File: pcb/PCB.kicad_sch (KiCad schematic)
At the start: 35 parts, among them J1 Conn_01x15, J2 USB_C_Receptacle_USB2.0, J3 Conn_01x15, J4 TC2030, J5 Conn_01x04, SW1 SW_Push, SW2 SW_Push, U1 SN65HVD230, U2 AMS1117-3.3, U3 STM32F103C8T6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

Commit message: Finished schematic
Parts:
- removed C10, C12, C8, C9: 100n, Capacitor_SMD:C_0402_1005Metric, symbol Device:C_Small
- removed C11, C2: 1u, Capacitor_SMD:C_0603_1608Metric, symbol Device:C_Small
- removed C5: 30p, Capacitor_SMD:C_0402_1005Metric, symbol Device:C_Small
- removed D1: YELLOW, LED_SMD:LED_0603_1608Metric, symbol Device:LED_Small
- removed D2: BLUE, LED_SMD:LED_0603_1608Metric, symbol Device:LED_Small
- removed FB1, FB2: 100R@100MHz, Resistor_SMD:R_0805_2012Metric, symbol Device:FerriteBead_Small
- removed J1, J3: Conn_01x15, Connector_PinHeader_2.54mm:PinHeader_1x15_P2.54mm_Vertical, symbol Connector_Generic:Conn_01x15
- removed J2: USB_C_Receptacle_USB2.0, Connector_USB:USB_C_Receptacle_HRO_TYPE-C-31-M-12, symbol Connector:USB_C_Receptacle_USB2.0
- removed J4: TC2030, Connector:Tag-Connect_TC2030-IDC-NL_2x03_P1.27mm_Vertical, symbol TC2030:TC2030
- removed J5: Conn_01x04, Connector_PinHeader_2.54mm:PinHeader_1x04_P2.54mm_Vertical, symbol Connector_Generic:Conn_01x04
- removed JP1: SolderJumper_Bridged, Jumper:SolderJumper-2_P1.3mm_Bridged_RoundedPad1.0x1.5mm, symbol Jumper:SolderJumper_2_Bridged
- removed R3: 120R, Resistor_SMD:R_0402_1005Metric, symbol Device:R_Small
- removed R4, R6, R7: 1k5, Resistor_SMD:R_0402_1005Metric, symbol Device:R_Small
- removed R5: 5k1, Resistor_SMD:R_0402_1005Metric, symbol Device:R_Small
- removed SW1, SW2: SW_Push, Button_Switch_SMD:SW_Push_1P1T_NO_CK_KSC7xxJ, symbol Switch:SW_Push
- removed U3: STM32F103C8T6, Package_QFP:LQFP-48_7x7mm_P0.5mm, symbol MCU_ST_STM32F1:STM32F103C8Tx
- removed Y1: 8MHz, Crystal:Crystal_SMD_5032-2Pin_5.0x3.2mm, symbol Device:Crystal_Small
- added C2, C5: 100uF, Capacitor_SMD:CP_Elec_6.3x7.7, symbol Device:C_Polarized_Small_US
- added D1: 15-25V, Diode_SMD:D_SMA, symbol Device:D_TVS
- added D16, D2: SP0502BAHT, Package_TO_SOT_SMD:SOT-23, symbol Power_Protection:SP0502BAHT
- added D3: ESDCAN02-2BWY, Package_TO_SOT_SMD:SOT-23, symbol Power_Protection:NUP2105L
- added J1: DTM1312PA12PBR008, DTM13-12PA-12PB:TE_DTM1312PA12PBR008, symbol DTM1312PA12PBR008:DTM1312PA12PBR008
- added R46: 470, Resistor_SMD:R_0603_1608Metric, symbol Device:R_Small
- C3: value 1u -> 2.2uF; footprint Capacitor_SMD:C_0603_1608Metric -> Capacitor_SMD:C_0805_2012Metric; LCSC C15849 -> (none)
- C4: value 4u7 -> 100nF; LCSC C19666 -> (none)
- C7: value 30p -> 100nF; footprint Capacitor_SMD:C_0402_1005Metric -> Capacitor_SMD:C_0603_1608Metric; LCSC C1570 -> (none)
- R1, R2: value 5k1 -> 470; footprint Resistor_SMD:R_0402_1005Metric -> Resistor_SMD:R_0603_1608Metric; LCSC C25905 -> (none)
- U2: LCSC C6186 -> (none)
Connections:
- net HSE_IN is gone; now on net +3V3: C7.1
- net +3V3: now also C5.1; no longer C3.1, C4.1, C6.1
- net CAN+: now also D3.1 (K), J1.B5
- net CAN-: now also D3.2 (K), J1.B6
- net GND: now also C2.2, C5.2, D1.2 (A2), D16.3 (A), D2.3 (A), J1.A11, J1.A2, J1.B10, J1.B3; no longer C6.2, R1.2, R2.1
- net UART_TX: now reaches R1.1
- net UART_TX: now also D2.1 (K), J1.B7
- net UART_RX: now reaches R2.2
- net UART_RX: now also D2.2 (K), J1.B8
- net at U1.5 (Vref): now also C6.1
- net VCC renamed +12V
- net +12V: now also C3.1, C4.1, C2.1, D1.1 (A1), J1.A10, J1.A3, J1.B4
- new net: C6.2, D3.3 (A)
- new net H0: J1.A12
- new net H1: J1.B1
- new net H2: J1.B2
- new net H3: J1.B11
- new net H4: J1.B12
- new net H5: J1.A1
- new net IO: D16.2 (K), J1.B9, R46.2
- new net L0: J1.A7
- new net L1: J1.A6
- new net L2: J1.A8
- new net L3: J1.A5
- new net L4: J1.A9
- new net L5: J1.A4
- new net STM32/GPIO: R46.1
- new net STM32/UART_RX: R2.1
- new net STM32/UART_TX: R1.2
- no-connect marks 9 -> 1
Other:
- added sheet High-side Channel 0 (highside.kicad_sch)
- added sheet High-side Channel 1 (highside.kicad_sch)
- added sheet High-side Channel 2 (highside.kicad_sch)
- added sheet High-side Channel 3 (highside.kicad_sch)
- added sheet High-side Channel 4 (highside.kicad_sch)
- added sheet High-side Channel 5 (highside.kicad_sch)
- added sheet Low-side channel 0 (lowside.kicad_sch)
- added sheet Low-side channel 1 (lowside.kicad_sch)
- added sheet Low-side channel 2 (lowside.kicad_sch)
- added sheet Low-side channel 3 (lowside.kicad_sch)
- added sheet Low-side channel 4 (lowside.kicad_sch)
- added sheet Low-side channel 5 (lowside.kicad_sch)
- added sheet STM32 (STM32.kicad_sch)
- note added: "3.3V Regulator"
- note removed: "1 = Bootloader, 0 = 'Run'"
- note removed: "1x bulk decoupling + 100nF per VDD pin"
- note removed: "3V3 regulator stable with 1uF output cap."
- note removed: "CL = 2 * (Cload - Cstray)"
- note removed: "GPIO Headers"
- note removed: "Ideally, boards should include GND for each signal pin and decoupling at power output pins (like +3V3)."
- note removed: "Low-pass filter for analog VDD"
- note removed: "Note: Best practice is to include a TVS protection diode near the connector (Refer to BCM design)."
- note removed: "Note: Power flags tell KiCad that a net is a power source. This avoids errors during Electrical Rules Check."
- note removed: "Optional termination resistor. See Brake Light schematic for a reference split-terminated design."
- note removed: "Programming/debug header. Place in an accessible location close to the mcu."
- note removed: "STM32F1 Microcontroller"
- note removed: "STM32F103 Reference Breakout Board"
- note removed: "STM32F103 requires external 1k5 pull-up on USB D+ line."
- note removed: "Tag Connect"
- note removed: "USB and Regulator"
- note removed: "USB device - leave shield floating."
- moved on the sheet: C1, U1

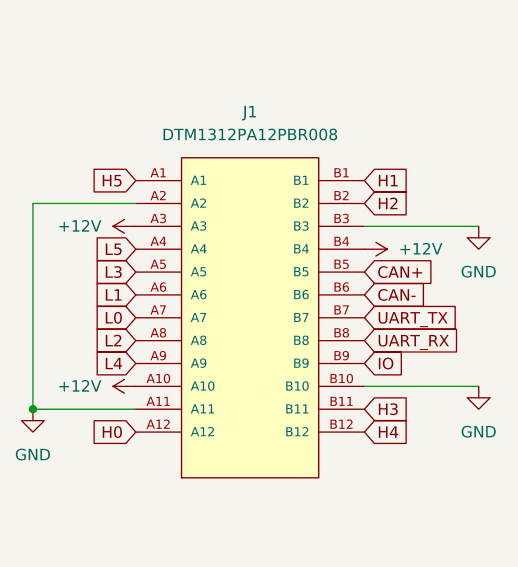
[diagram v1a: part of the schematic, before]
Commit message: Started layout
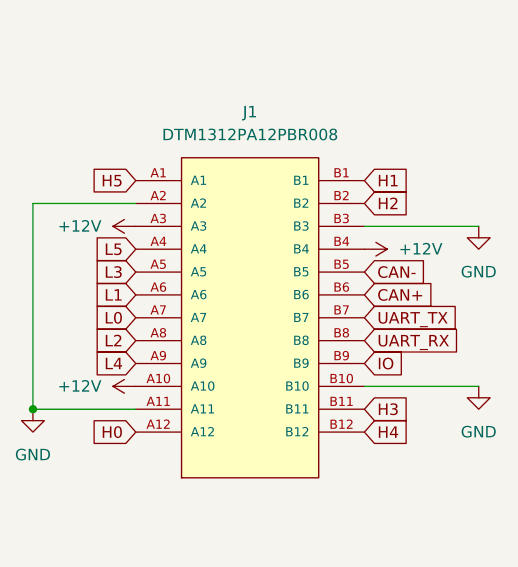
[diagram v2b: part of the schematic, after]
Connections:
- net CAN+: now also J1.B6; no longer J1.B5
- net CAN-: now also J1.B5; no longer J1.B6
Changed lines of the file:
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@@
     )
   )
-  (global_label "CAN-" (shape input) (at 234.95 87.63 0) (fields_autoplaced)
-    (effects (font (size 1.27 1.27)) (justify left))
-    (property "Intersheet References" "${INTERSHEET_REFS}" (id 0) (at 242.6245 87.5506 0)
+  (global_label "CAN-" (shape input) (at 234.95 85.09 0) (fields_autoplaced)
+    (effects (font (size 1.27 1.27)) (justify left))
+    (property "Intersheet References" "${INTERSHEET_REFS}" (id 0) (at 242.6245 85.0106 0)
       (effects (font (size 1.27 1.27)) (justify left) hide)
     )
@@
     )
   )
-  (global_label "CAN+" (shape input) (at 234.95 85.09 0) (fields_autoplaced)
-    (effects (font (size 1.27 1.27)) (justify left))
-    (property "Intersheet References" "${INTERSHEET_REFS}" (id 0) (at 242.6245 85.0106 0)
+  (global_label "CAN+" (shape input) (at 234.95 87.63 0) (fields_autoplaced)
+    (effects (font (size 1.27 1.27)) (justify left))
+    (property "Intersheet References" "${INTERSHEET_REFS}" (id 0) (at 242.6245 87.5506 0)
       (effects (font (size 1.27 1.27)) (justify left) hide)
     )
@@
       (reference "#PWR010") (unit 1) (value "+3V3") (footprint "")
     )
-    (path "/1d08d960-24a6-461a-b4f3-543e0f014558/898ca406-6b9b-4516-8b9f-8dbe52b67a30"
-      (reference "#PWR011") (unit 1) (value "+3V3") (footprint "")
-    )
     (path "/1d08d960-24a6-461a-b4f3-543e0f014558/cdb9daf3-cf5d-4c6d-be96-1ffa36850e9c"
       (reference "#PWR012") (unit 1) (value "GND") (footprint "")
@@
       (reference "#PWR016") (unit 1) (value "GND") (footprint "")
     )
-    (path "/1d08d960-24a6-461a-b4f3-543e0f014558/8d4a818a-3390-4839-a6b7-95b9c5c5c590"
-      (reference "#PWR017") (unit 1) (value "+3V3") (footprint "")
-    )
     (path "/1d08d960-24a6-461a-b4f3-543e0f014558/4f03b956-f8f7-4414-a0fd-bef829742b97"
       (reference "#PWR018") (unit 1) (value "+3V3") (footprint "")
@@
       (reference "#PWR0107") (unit 1) (value "GND") (footprint "")
     )
+    (path "/1d08d960-24a6-461a-b4f3-543e0f014558/06a93daa-b6e2-4fc1-8d56-459e69185f23"
+      (reference "#PWR?") (unit 1) (value "+3V3") (footprint "")
+    )
     (path "/f95b01db-0883-42ec-8156-6165babeddd5"
       (reference "C1") (unit 1) (value "100n") (footprint "Capacitor_SMD:C_0402_1005Metric")
@@
       (reference "R2") (unit 1) (value "470") (footprint "Resistor_SMD:R_0603_1608Metric")
     )
-    (path "/1d08d960-24a6-461a-b4f3-543e0f014558/0131c735-2ce0-4af4-b13f-c6cd7605fdbe"
-      (reference "R3") (unit 1) (value "5k1") (footprint "Resistor_SMD:R_0603_1608Metric")
-    )
     (path "/ae4e646b-9a05-48be-bf6c-68da84d9d52e/8b021fae-fb4b-4f70-a5f9-b9a251a77706"
       (reference "R4") (unit 1) (value "4.7k") (footprint "Resistor_SMD:R_0603_1608Metric")
@@
       (reference "R46") (unit 1) (value "470") (footprint "Resistor_SMD:R_0603_1608Metric")
     )
-    (path "/1d08d960-24a6-461a-b4f3-543e0f014558/05d4e824-5e78-44e6-a3d5-56fd3c2fb254"
-      (reference "SW1") (unit 1) (value "SW_Push") (footprint "Button_Switch_SMD:SW_Push_1P1T_NO_CK_KSC7xxJ")
-    )
-    (path "/1d08d960-24a6-461a-b4f3-543e0f014558/5248a7c9-e2fa-4657-959b-22392763c96f"
-      (reference "SW2") (unit 1) (value "SW_Push") (footprint "Button_Switch_SMD:SW_Push_1P1T_NO_CK_KSC7xxJ")
-    )
     (path "/ae917481-13f0-43e4-9745-414651f8776f"

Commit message: Worked on layout
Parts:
- renumbered C2 to C1, C1 to C2, D16 to D4, R46 to R3

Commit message: Worked on layout some more
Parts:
- added H1: MountingHole, MountingHole:MountingHole_3.2mm_M3, symbol Mechanical:MountingHole
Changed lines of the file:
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@@
     (pin "2")
+  )
+  (symbol (lib_id "Mechanical:MountingHole") (at 213.36 114.3 0) (unit 1)
+    (in_bom yes) (on_board yes) (fields_autoplaced)
+    (property "Reference" "H1" (id 0) (at 215.9 113.0299 0)
+      (effects (font (size 1.27 1.27)) (justify left))
+    )
+    (property "Value" "MountingHole" (id 1) (at 215.9 115.5699 0)
+      (effects (font (size 1.27 1.27)) (justify left))
+    )
+    (property "Footprint" "MountingHole:MountingHole_3.2mm_M3" (id 2) (at 213.36 114.3 0)
+      (effects (font (size 1.27 1.27)) hide)
+    )
+    (property "Datasheet" "~" (id 3) (at 213.36 114.3 0)
+      (effects (font (size 1.27 1.27)) hide)
+    )
   )
   (symbol (lib_id "power:+3V3") (at 48.26 151.13 0) (unit 1)
@@
       (reference "FB1") (unit 1) (value "100R@100MHz") (footprint "Resistor_SMD:R_0805_2012Metric")
     )
+    (path "/93d54b21-883b-4205-a288-bae6cc44c1e8"
+      (reference "H1") (unit 1) (value "MountingHole") (footprint "MountingHole:MountingHole_3.2mm_M3")
+    )
     (path "/d6bde4d9-ffb7-4d4e-ae84-524e1254604a"

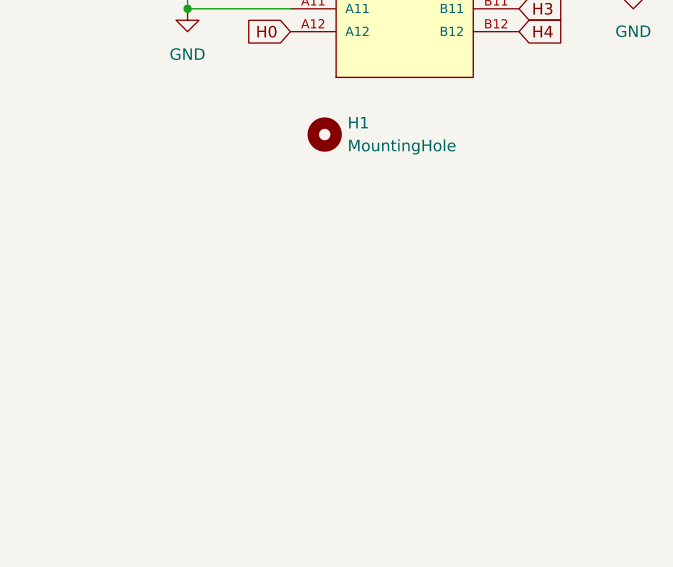
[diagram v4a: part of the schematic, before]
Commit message: Added debug/test header
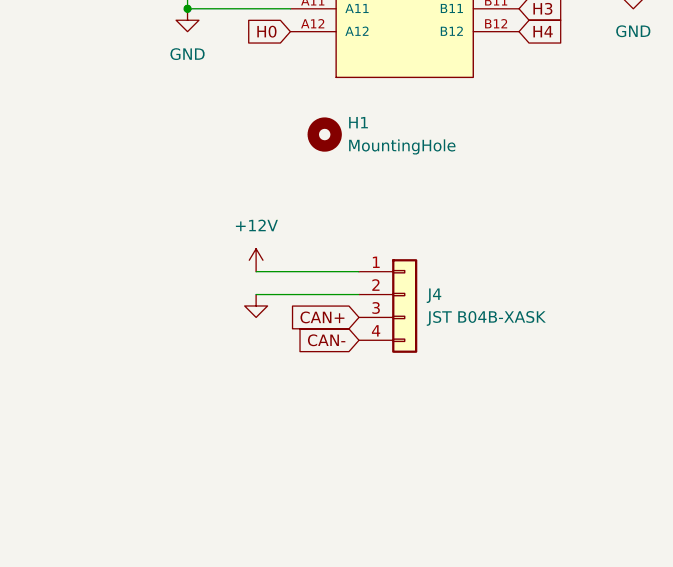
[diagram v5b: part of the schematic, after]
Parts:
- added J4: JST B04B-XASK, Connector_JST:JST_XA_B04B-XASK-1_1x04_P2.50mm_Vertical, symbol Connector_Generic:Conn_01x04
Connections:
- net +12V: now also J4.1 (Pin_1)
- net CAN+: now also J4.3 (Pin_3)
- net CAN-: now also J4.4 (Pin_4)
- net GND: now also J4.2 (Pin_2)
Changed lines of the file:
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@@
+    (stroke (width 0) (type default) (color 0 0 0 0))
+  )
+  (wire (pts (xy 205.74 132.08) (xy 217.17 132.08))
     (stroke (width 0) (type default) (color 0 0 0 0))
   )
   (wire (pts (xy 85.09 119.38) (xy 85.09 121.92))
+    (stroke (width 0) (type default) (color 0 0 0 0))
+  )
+  (wire (pts (xy 205.74 129.54) (xy 217.17 129.54))
     (stroke (width 0) (type default) (color 0 0 0 0))
   )
@@
     (property "Intersheet References" "${INTERSHEET_REFS}" (id 0) (at 159.5907 59.6106 0)
       (effects (font (size 1.27 1.27)) (justify left) hide)
+    )
+  )
+  (global_label "CAN+" (shape input) (at 217.17 134.62 180) (fields_autoplaced)
+    (effects (font (size 1.27 1.27)) (justify right))
+    (property "Intersheet References" "${INTERSHEET_REFS}" (id 0) (at 209.4955 134.5406 0)
+      (effects (font (size 1.27 1.27)) (justify right) hide)
     )
   )
@@
     )
   )
+  (global_label "CAN-" (shape input) (at 217.17 137.16 180) (fields_autoplaced)
+    (effects (font (size 1.27 1.27)) (justify right))
+    (property "Intersheet References" "${INTERSHEET_REFS}" (id 0) (at 209.4955 137.2394 0)
+      (effects (font (size 1.27 1.27)) (justify right) hide)
+    )
+  )
   (global_label "L0" (shape input) (at 154.94 25.4 0) (fields_autoplaced)
     (effects (font (size 1.27 1.27)) (justify left))
@@
     (pin "1")
     (pin "2")
+  )
+  (symbol (lib_id "power:GND") (at 205.74 132.08 0) (mirror y) (unit 1)
+    (in_bom yes) (on_board yes) (fields_autoplaced)
+    (property "Reference" "#PWR0101" (id 0) (at 205.74 138.43 0)
+      (effects (font (size 1.27 1.27)) hide)
+    )
+    (property "Value" "GND" (id 1) (at 205.74 137.16 0)
+      (effects (font (size 1.27 1.27)) hide)
+    )
+    (property "Footprint" "" (id 2) (at 205.74 132.08 0)
+      (effects (font (size 1.27 1.27)) hide)
+    )
+    (property "Datasheet" "" (id 3) (at 205.74 132.08 0)
+      (effects (font (size 1.27 1.27)) hide)
+    )
+    (pin "1")
   )
   (symbol (lib_id "power:GND") (at 247.65 80.01 0) (mirror y) (unit 1)
@@
     )
     (property "Datasheet" "" (id 3) (at 198.12 100.33 0)
+      (effects (font (size 1.27 1.27)) hide)
+    )
+    (pin "1")
+  )
+  (symbol (lib_id "power:+12V") (at 205.74 129.54 0) (unit 1)
+    (in_bom yes) (on_board yes) (fields_autoplaced)
+    (property "Reference" "#PWR0102" (id 0) (at 205.74 133.35 0)
+      (effects (font (size 1.27 1.27)) hide)
+    )
+    (property "Value" "+12V" (id 1) (at 205.74 124.46 0))
+    (property "Footprint" "" (id 2) (at 205.74 129.54 0)
+      (effects (font (size 1.27 1.27)) hide)
+    )
+    (property "Datasheet" "" (id 3) (at 205.74 129.54 0)
       (effects (font (size 1.27 1.27)) hide)
     )
@@
     (pin "1")
   )
+  (symbol (lib_id "Connector_Generic:Conn_01x04") (at 222.25 132.08 0) (unit 1)
+    (in_bom yes) (on_board yes) (fields_autoplaced)
+    (property "Reference" "J4" (id 0) (at 224.79 132.0799 0)
+      (effects (font (size 1.27 1.27)) (justify left))
+    )
+    (property "Value" "JST B04B-XASK" (id 1) (at 224.79 134.6199 0)
+      (effects (font (size 1.27 1.27)) (justify left))
+    )
+    (property "Footprint" "Connector_JST:JST_XA_B04B-XASK-1_1x04_P2.50mm_Vertical" (id 2) (at 222.25 132.08 0)
+      (effects (font (size 1.27 1.27)) hide)
+    )
+    (property "Datasheet" "~" (id 3) (at 222.25 132.08 0)
+      (effects (font (size 1.27 1.27)) hide)
+    )
+    (pin "1")
+    (pin "2")
+    (pin "3")
+    (pin "4")
+  )
   (symbol (lib_id "power:+12V") (at 35.56 55.88 0) (unit 1)
     (in_bom yes) (on_board yes) (fields_autoplaced)
@@
       (reference "#PWR083") (unit 1) (value "GND") (footprint "")
     )
+    (path "/0c94e726-3b2b-431d-86e8-075ec99da1a2"
+      (reference "#PWR0101") (unit 1) (value "GND") (footprint "")
+    )
+    (path "/b7d8f29b-45a0-437f-bfe0-3b89af56ec40"
+      (reference "#PWR0102") (unit 1) (value "+12V") (footprint "")
+    )
     (path "/ab10e1c5-1025-4062-b932-6116c1e566e3"
       (reference "C1") (unit 1) (value "100uF") (footprint "Capacitor_SMD:CP_Elec_6.3x7.7")
@@
       (reference "J3") (unit 1) (value "Conn_02x08_Top_Bottom") (footprint "Connector_PinHeader_2.54mm:PinHeader_2x08_P2.54mm_Vertical")
     )
+    (path "/f52b110f-daa8-4882-96c6-b4e6e913a7c5"
+      (reference "J4") (unit 1) (value "JST B04B-XASK") (footprint "Connector_JST:JST_XA_B04B-XASK-1_1x04_P2.50mm_Vertical")
+    )
     (path "/812bafd9-a772-4dd5-bf65-a63d4d3b191c/92b722ea-ca79-4799-90e4-1fd9f27fa099"

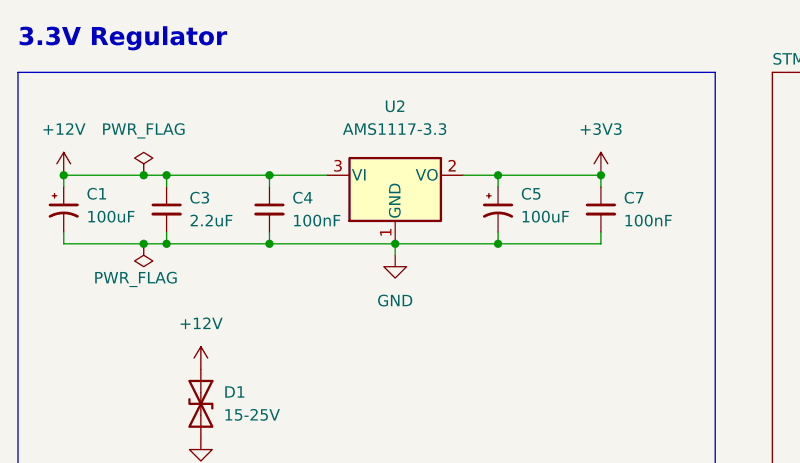
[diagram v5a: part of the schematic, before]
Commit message: Switched to non-sketchy regulator
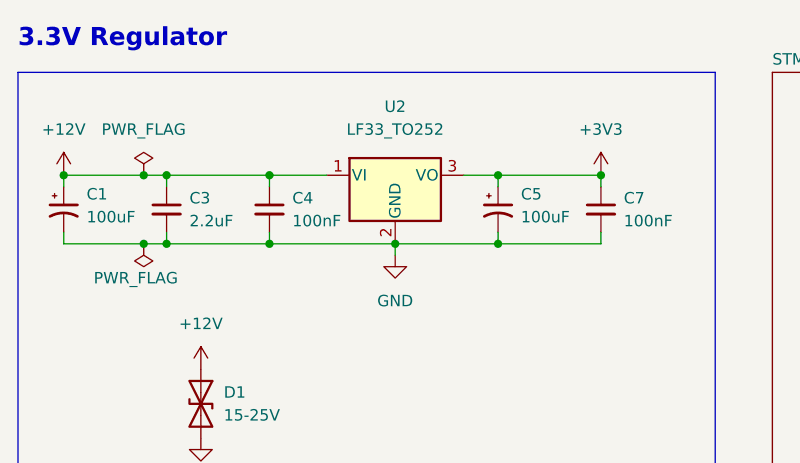
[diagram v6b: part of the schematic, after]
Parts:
- removed U2: AMS1117-3.3, Package_TO_SOT_SMD:SOT-223-3_TabPin2, symbol Regulator_Linear:AMS1117-3.3
- added U2: LF33_TO252, Package_TO_SOT_SMD:TO-252-2, symbol Regulator_Linear:LF33_TO252
- J1: footprint DTM13-12PA-12PB:TE_DTM1312PA12PBR008 -> TE_DTM1312PA12PBR008
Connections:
- net +12V: now also U2.1 (VI)
- net +3V3: now also U2.3 (VO)
- net GND: now also U2.2 (GND)
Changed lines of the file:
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@@
     (pin "1")
-  )
-  (symbol (lib_id "Regulator_Linear:AMS1117-3.3") (at 57.15 34.29 0) (unit 1)
-    (in_bom yes) (on_board yes) (fields_autoplaced)
-    (property "Reference" "U2" (id 0) (at 57.15 26.67 0))
-    (property "Value" "AMS1117-3.3" (id 1) (at 57.15 29.21 0))
-    (property "Footprint" "Package_TO_SOT_SMD:SOT-223-3_TabPin2" (id 2) (at 57.15 29.21 0)
-      (effects (font (size 1.27 1.27)) hide)
-    )
-    (property "Datasheet" "http://www.advanced-monolithic.com/pdf/ds1117.pdf" (id 3) (at 59.69 40.64 0)
-      (effects (font (size 1.27 1.27)) hide)
-    )
-    (pin "1")
-    (pin "2")
-    (pin "3")
   )
   (symbol (lib_id "Device:R_Small") (at 88.9 93.98 270) (unit 1)
@@
     (property "Reference" "J1" (id 0) (at 222.25 67.31 0))
     (property "Value" "DTM1312PA12PBR008" (id 1) (at 222.25 69.85 0))
-    (property "Footprint" "DTM13-12PA-12PB:TE_DTM1312PA12PBR008" (id 2) (at 222.25 87.63 0)
+    (property "Footprint" "TE_DTM1312PA12PBR008" (id 2) (at 222.25 87.63 0)
       (effects (font (size 1.27 1.27)) (justify left bottom) hide)
     )
@@
     (pin "B9")
   )
+  (symbol (lib_id "Regulator_Linear:LF33_TO252") (at 57.15 34.29 0) (unit 1)
+    (in_bom yes) (on_board yes) (fields_autoplaced)
+    (property "Reference" "U2" (id 0) (at 57.15 26.67 0))
+    (property "Value" "LF33_TO252" (id 1) (at 57.15 29.21 0))
+    (property "Footprint" "Package_TO_SOT_SMD:TO-252-2" (id 2) (at 57.15 28.575 0)
+      (effects (font (size 1.27 1.27) italic) hide)
+    )
+    (property "Datasheet" "http://www.st.com/content/ccc/resource/technical/document/datasheet/c4/0e/7e/2a/be/bc/4c/bd/CD00000546.pdf/files/CD00000546.pdf/jcr:content/translations/en.CD00000546.pdf" (id 3) (at 57.15 35.56 0)
+      (effects (font (size 1.27 1.27)) hide)
+    )
+    (pin "1")
+    (pin "2")
+    (pin "3")
+  )
   (symbol (lib_id "power:+3V3") (at 80.01 34.29 0) (unit 1)
     (in_bom yes) (on_board yes) (fields_autoplaced)
@@
     )
     (path "/d6bde4d9-ffb7-4d4e-ae84-524e1254604a"
-      (reference "J1") (unit 1) (value "DTM1312PA12PBR008") (footprint "DTM13-12PA-12PB:TE_DTM1312PA12PBR008")
+      (reference "J1") (unit 1) (value "DTM1312PA12PBR008") (footprint "TE_DTM1312PA12PBR008")
     )
     (path "/1d08d960-24a6-461a-b4f3-543e0f014558/86b61b36-28e1-4d1c-9f8e-bc6fc9a33198"
@@
       (reference "U1") (unit 1) (value "SN65HVD230") (footprint "Package_SO:SOIC-8_3.9x4.9mm_P1.27mm")
     )
-    (path "/408fd4b5-05ec-438d-b490-807f55bf3d89"
-      (reference "U2") (unit 1) (value "AMS1117-3.3") (footprint "Package_TO_SOT_SMD:SOT-223-3_TabPin2")
+    (path "/dd756c3f-714a-405f-b9b5-c826632b53e6"
+      (reference "U2") (unit 1) (value "LF33_TO252") (footprint "Package_TO_SOT_SMD:TO-252-2")
     )
     (path "/1d08d960-24a6-461a-b4f3-543e0f014558/090d23cc-6257-44a6-97f3-4018e9a149d0"
